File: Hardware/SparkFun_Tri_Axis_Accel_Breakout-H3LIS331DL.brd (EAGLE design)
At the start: 20.3 x 20.3 mm, 23 parts, among them U1 H3LIS331DL

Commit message: Aesthetic touch ups before review
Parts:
- moved JP6 38.1 mm to (-19.1, 5.08), flipped to the bottom
- moved JP7 38.1 mm to (-19.1, 5.08), flipped to the top
- moved JP10 35.6 mm to (-17.8, 17.8), flipped to the bottom
- moved JP8 35.6 mm to (-17.8, 2.54), flipped to the bottom
- moved JP3 34.0 mm to (-17.0, 7.11), flipped to the bottom
- moved JP2 32.0 mm to (-16.0, 13.2), flipped to the bottom
- moved R1 30.5 mm to (-15.2, 6.48), flipped to the bottom
- moved R4 27.9 mm to (-14.0, 14.0), flipped to the bottom
- moved R2 22.1 mm to (-11.0, 5.97), flipped to the bottom
- moved R3 22.1 mm to (-11.0, 4.19), flipped to the bottom
- moved U1 20.3 mm to (-10.2, 10.2), flipped to the bottom
- moved JP1 15.2 mm to (-7.62, 5.08), flipped to the bottom
- moved C1 12.7 mm to (-6.35, 10.2), flipped to the bottom
- moved J1 12.7 mm to (-6.35, 19.1), flipped to the bottom
- moved J2 12.7 mm to (-6.35, 1.27), flipped to the bottom
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
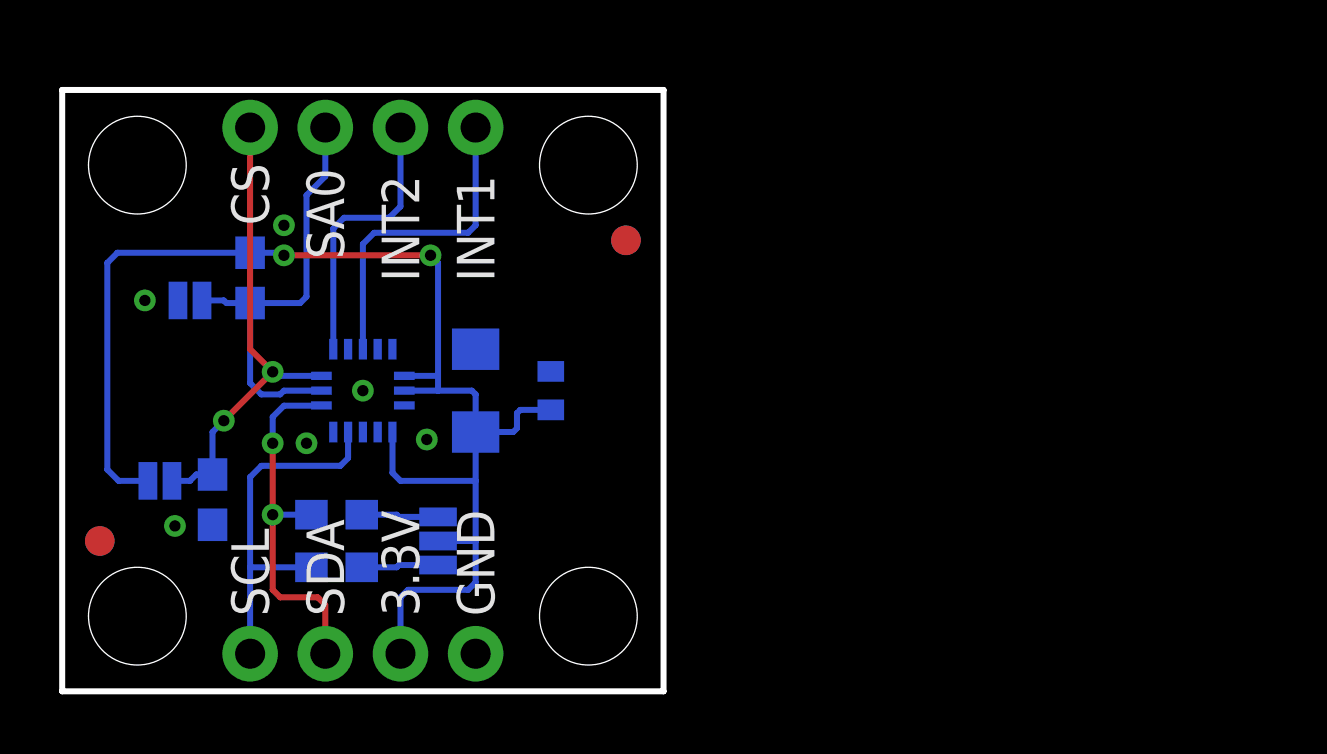
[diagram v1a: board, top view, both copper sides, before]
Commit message: Replace some components with newer versions
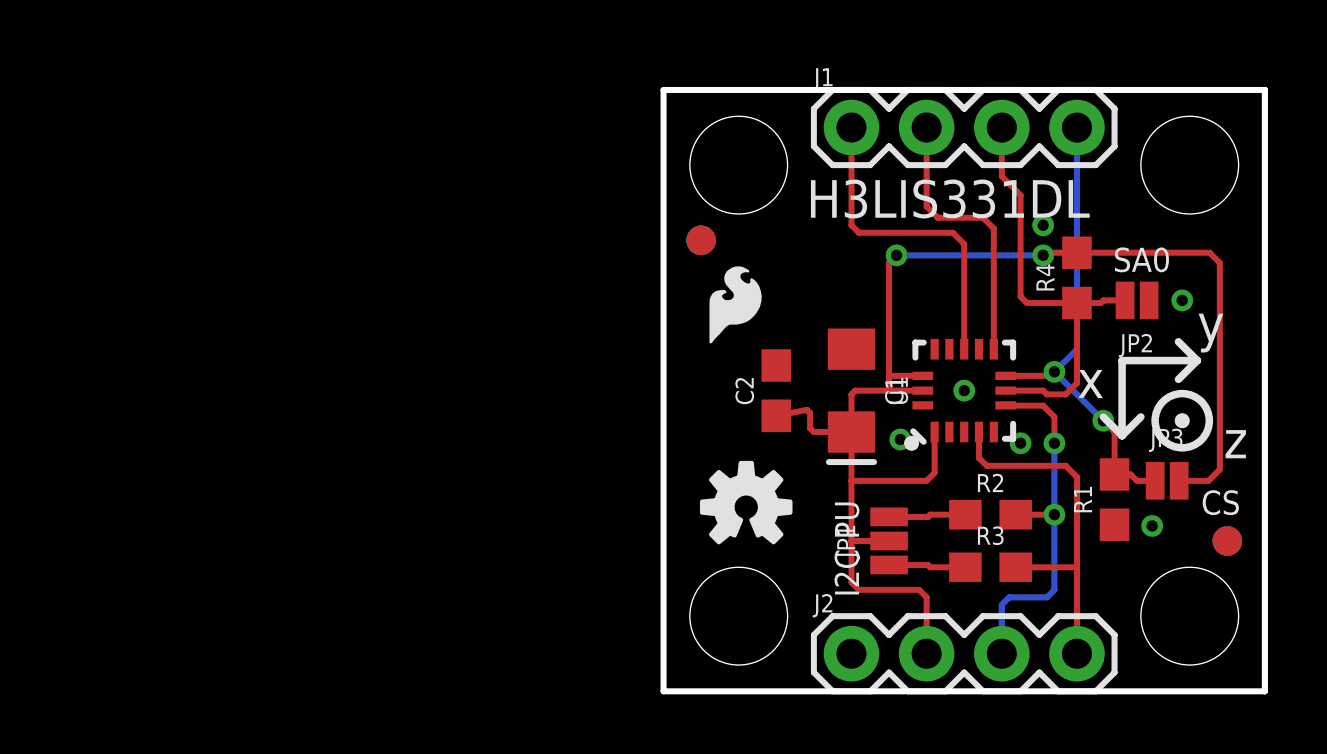
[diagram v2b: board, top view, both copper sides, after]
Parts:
- C1: device SparkFun:EIA3216 -> SparkFun-Capacitors:EIA3216
- C2: device SparkFun:0402-CAP -> SparkFun-Capacitors:0603
- moved JP6 38.1 mm to (19.1, 5.08), flipped to the top
- moved JP7 38.1 mm to (19.1, 5.08), flipped to the bottom
- moved JP10 35.6 mm to (17.8, 17.8), flipped to the top
- moved JP8 35.6 mm to (17.8, 2.54), flipped to the top
- moved JP3 34.0 mm to (17.0, 7.11), flipped to the top
- moved JP2 32.0 mm to (16.0, 13.2), flipped to the top
- moved R1 30.5 mm to (15.2, 6.48), flipped to the top
- moved R4 27.9 mm to (14.0, 14.0), flipped to the top
- moved R2 22.1 mm to (11.0, 5.97), flipped to the top
- moved R3 22.1 mm to (11.0, 4.19), flipped to the top
- moved U1 20.3 mm to (10.2, 10.2), flipped to the top
- moved JP1 15.2 mm to (7.62, 5.08), flipped to the top
- moved C1 12.7 mm to (6.35, 10.2), flipped to the top
- moved J1 12.7 mm to (6.35, 19.1), flipped to the top
- moved J2 12.7 mm to (6.35, 1.27), flipped to the top
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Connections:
- net 3.3V: now also C1.+; no longer C1.A
- net GND: now also C1.-; no longer C1.C

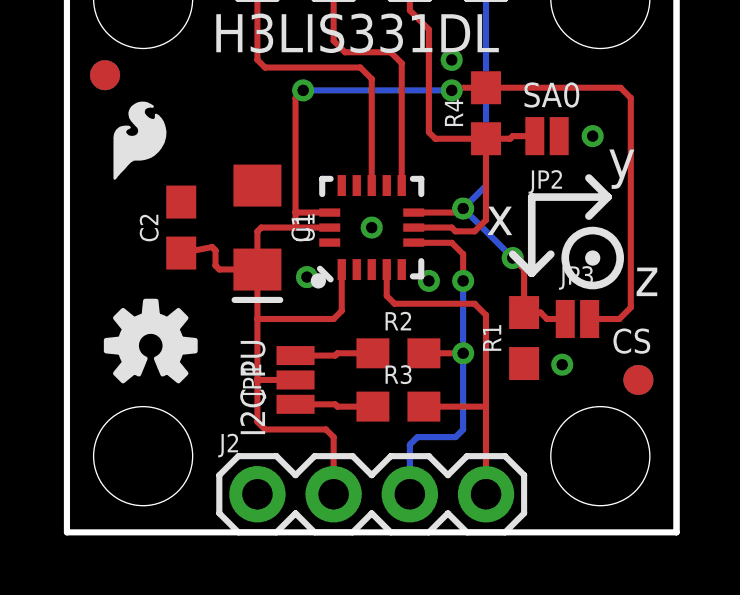
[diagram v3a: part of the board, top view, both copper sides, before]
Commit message: Improvements post review
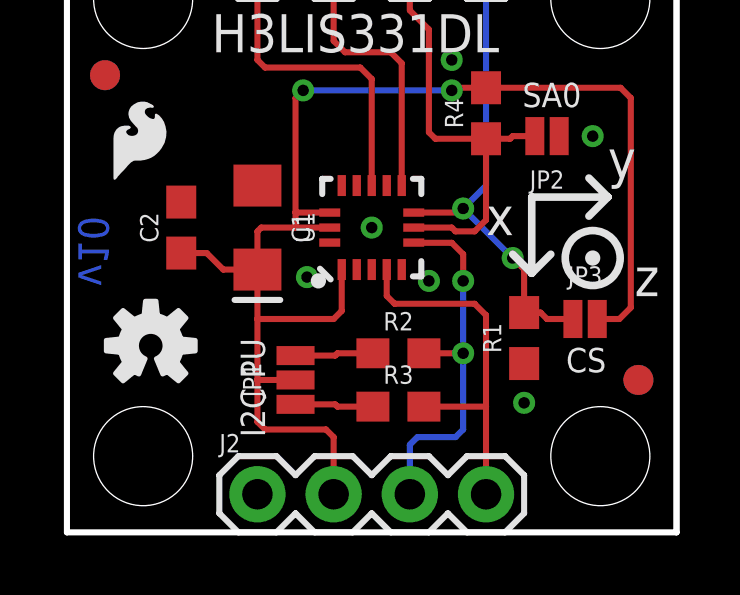
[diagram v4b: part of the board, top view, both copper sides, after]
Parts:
- moved FRAME1 8.98 mm to (1.27, -19.1)
- moved JP3 0.25 mm to (17.3, 7.11)
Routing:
- net 3.3V: track 47.6 -> 47.0 mm
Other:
- board text added: "v10"
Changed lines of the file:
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@@
 <layer number="20" name="Dimension" color="15" fill="1" visible="yes" active="yes"/>
 <layer number="21" name="tPlace" color="16" fill="1" visible="yes" active="yes"/>
-<layer number="22" name="bPlace" color="14" fill="1" visible="yes" active="yes"/>
+<layer number="22" name="bPlace" color="14" fill="1" visible="no" active="yes"/>
 <layer number="23" name="tOrigins" color="15" fill="1" visible="yes" active="yes"/>
-<layer number="24" name="bOrigins" color="15" fill="1" visible="yes" active="yes"/>
-<layer number="25" name="tNames" color="7" fill="1" visible="no" active="yes"/>
+<layer number="24" name="bOrigins" color="15" fill="1" visible="no" active="yes"/>
+<layer number="25" name="tNames" color="7" fill="1" visible="yes" active="yes"/>
 <layer number="26" name="bNames" color="7" fill="1" visible="no" active="yes"/>
 <layer number="27" name="tValues" color="7" fill="1" visible="no" active="yes"/>
@@
 <layer number="43" name="vRestrict" color="2" fill="10" visible="no" active="yes"/>
 <layer number="44" name="Drills" color="7" fill="1" visible="no" active="yes"/>
-<layer number="45" name="Holes" color="7" fill="1" visible="yes" active="yes"/>
+<layer number="45" name="Holes" color="7" fill="1" visible="no" active="yes"/>
 <layer number="46" name="Milling" color="3" fill="1" visible="no" active="yes"/>
 <layer number="47" name="Measures" color="7" fill="1" visible="no" active="yes"/>
 <layer number="48" name="Document" color="7" fill="1" visible="no" active="yes"/>
 <layer number="49" name="Reference" color="7" fill="1" visible="no" active="yes"/>
-<layer number="51" name="tDocu" color="6" fill="1" visible="yes" active="yes"/>
+<layer number="51" name="tDocu" color="6" fill="1" visible="no" active="yes"/>
 <layer number="52" name="bDocu" color="7" fill="1" visible="no" active="yes"/>
 <layer number="3" name="Route3" color="4" fill="3" visible="no" active="no"/>
@@
 <text x="18.034" y="11.811" size="1.27" layer="21" font="vector" ratio="15">y</text>
 <text x="18.923" y="7.874" size="1.27" layer="21" font="vector" ratio="15">z</text>
-<text x="30.48" y="-10.16" size="1.778" layer="51" font="vector" ratio="15">Mike Hord</text>
+<text x="31.75" y="-19.05" size="1.778" layer="51" font="vector" ratio="15">Mike Hord</text>
 <text x="6.604" y="3.175" size="0.8128" layer="21" font="vector" ratio="15" rot="R90">I2C PU</text>
 <text x="17.145" y="14.986" size="0.8128" layer="21" font="vector" ratio="15" rot="R180">SA0</text>
@@
 <text x="-2.413" y="10.16" size="0.8128" layer="47" font="vector" ratio="15" rot="R270">typ.</text>
 <text x="10.16" y="-1.27" size="0.8128" layer="47" font="vector" ratio="15">Units in inches</text>
-<text x="18.161" y="5.969" size="0.8128" layer="21" font="vector" ratio="15">CS</text>
+<text x="16.637" y="5.334" size="0.8128" layer="21" font="vector" ratio="15">CS</text>
 <wire x1="20.32" y1="20.32" x2="20.32" y2="0" width="0.2032" layer="20"/>
+<text x="1.397" y="10.541" size="1.016" layer="16" font="vector" ratio="15" rot="MR270">v10</text>
+<wire x1="9.398" y1="11.938" x2="9.398" y2="11.303" width="0.1524" layer="41"/>
 </plain>
 <attributes>
@@
 <attribute name="PROD_ID" value="RES-07857" x="11.049" y="4.191" size="1.778" layer="27" font="vector" ratio="15" display="off"/>
 </element>
-<element name="FRAME1" library="SparkFun-Aesthetics" package="CREATIVE_COMMONS" value="FRAME-LETTER" x="0" y="-10.16"/>
+<element name="FRAME1" library="SparkFun-Aesthetics" package="CREATIVE_COMMONS" value="FRAME-LETTER" x="1.27" y="-19.05"/>
 <element name="LOGO2" library="SparkFun-Aesthetics" package="OSHW-LOGO-S" value="OSHW-LOGOS" x="2.794" y="6.223"/>
 <element name="LOGO1" library="SparkFun-Aesthetics" package="SFE_LOGO_FLAME_.1" value="SFE_LOGO_FLAME.1_INCH" x="1.27" y="11.43"/>
@@
 <attribute name="PROD_ID" value="RES-00824" x="11.43" y="6.477" size="0.8128" layer="27" font="vector" ratio="15" rot="R90" display="off"/>
 </element>
-<element name="JP3" library="SparkFun-Jumpers" package="SMT-JUMPER_2_NC_PASTE_NO-SILK" value="JUMPER-SMT_2_NC_PASTE_NO-SILK" x="17.018" y="7.112"/>
+<element name="JP3" library="SparkFun-Jumpers" package="SMT-JUMPER_2_NC_PASTE_NO-SILK" value="JUMPER-SMT_2_NC_PASTE_NO-SILK" x="17.272" y="7.112"/>
 </elements>
 <signals>
@@
 <wire x1="15.24" y1="7.327" x2="15.787" y2="7.327" width="0.2032" layer="1"/>
 <wire x1="15.787" y1="7.327" x2="16.002" y2="7.112" width="0.2032" layer="1"/>
-<wire x1="16.6116" y1="7.112" x2="16.002" y2="7.112" width="0.2032" layer="1"/>
+<wire x1="16.8656" y1="7.112" x2="16.002" y2="7.112" width="0.2032" layer="1"/>
 <wire x1="15.24" y1="7.327" x2="15.24" y2="8.763" width="0.2032" layer="1"/>
 <wire x1="15.24" y1="8.763" x2="14.859" y2="9.144" width="0.2032" layer="1"/>
@@
 <via x="17.526" y="13.208" extent="1-16" drill="0.381"/>
 <contactref element="R1" pad="1"/>
-<via x="16.51" y="5.588" extent="1-16" drill="0.381"/>
+<via x="15.24" y="4.318" extent="1-16" drill="0.381"/>
 <via x="12.827" y="15.748" extent="1-16" drill="0.381"/>
 </signal>
@@
 <contactref element="R4" pad="2"/>
 <contactref element="JP1" pad="2"/>
-<wire x1="3.81" y1="9.31" x2="4.841" y2="9.51" width="0.2032" layer="1"/>
-<wire x1="4.841" y1="9.51" x2="4.953" y2="9.398" width="0.2032" layer="1"/>
-<wire x1="4.953" y1="9.398" x2="4.953" y2="8.89" width="0.2032" layer="1"/>
-<wire x1="4.953" y1="8.89" x2="5.08" y2="8.763" width="0.2032" layer="1"/>
-<wire x1="5.08" y1="8.763" x2="6.347" y2="8.763" width="0.2032" layer="1"/>
-<wire x1="6.347" y1="8.763" x2="6.35" y2="8.76" width="0.2032" layer="1"/>
 <wire x1="6.35" y1="8.76" x2="6.35" y2="7.112" width="0.2032" layer="1"/>
 <wire x1="6.35" y1="7.112" x2="6.35" y2="5.08" width="0.2032" layer="1"/>
@@
 <wire x1="18.796" y1="14.478" x2="18.796" y2="7.493" width="0.2032" layer="1"/>
 <wire x1="18.796" y1="7.493" x2="18.415" y2="7.112" width="0.2032" layer="1"/>
-<wire x1="18.415" y1="7.112" x2="17.4244" y2="7.112" width="0.2032" layer="1"/>
+<wire x1="18.415" y1="7.112" x2="17.6784" y2="7.112" width="0.2032" layer="1"/>
+<wire x1="3.81" y1="9.31" x2="4.66" y2="9.31" width="0.2032" layer="1"/>
+<wire x1="4.66" y1="9.31" x2="5.21" y2="8.76" width="0.2032" layer="1"/>
+<wire x1="6.35" y1="8.76" x2="5.21" y2="8.76" width="0.2032" layer="1"/>
 </signal>
 <signal name="N$1">
@@
 </signal>
 </signals>
+<errors>
+</errors>
 </board>
 </drawing>
